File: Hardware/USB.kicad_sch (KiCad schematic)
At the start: 14 parts, among them J7 ??, U7 CP2102N-A02-GQFN24

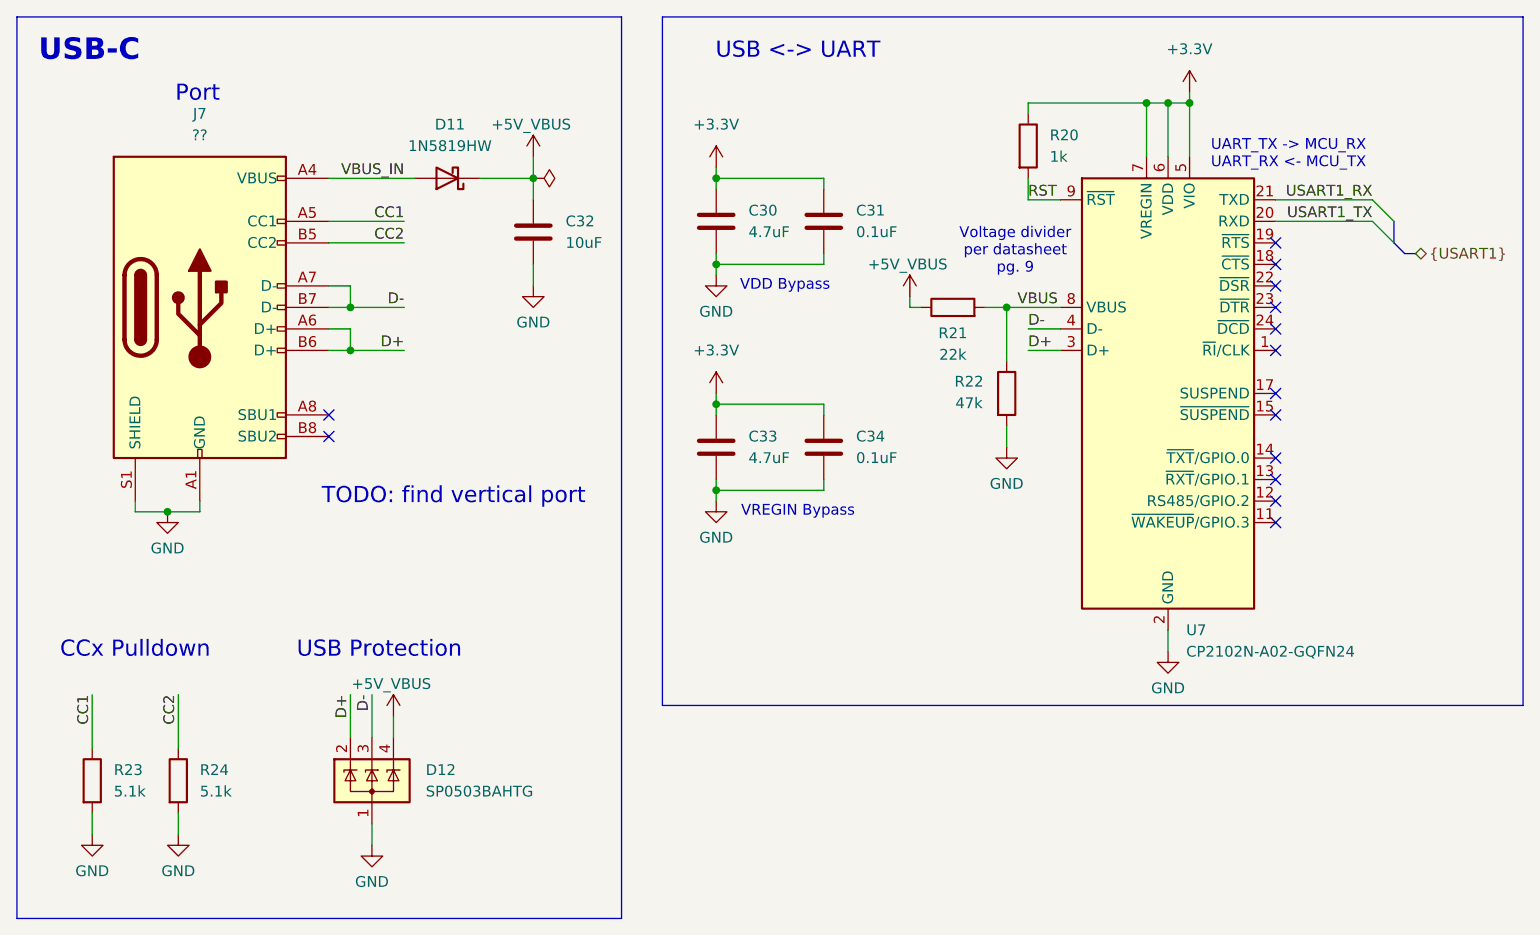
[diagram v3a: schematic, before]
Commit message: 0603 footprints
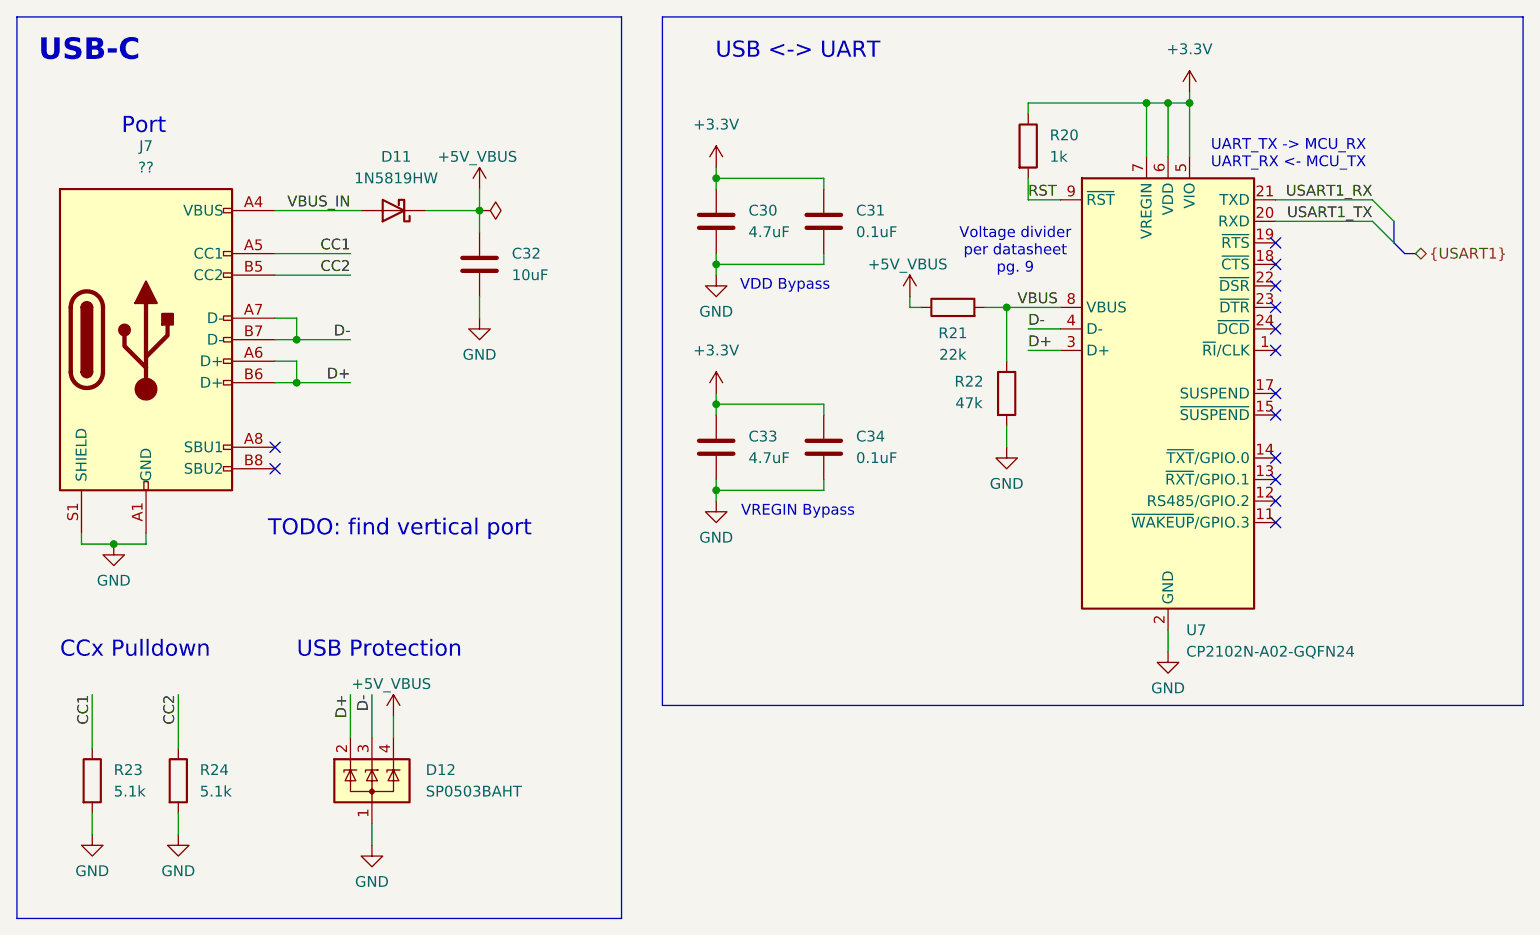
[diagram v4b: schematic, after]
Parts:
- removed D12: SP0503BAHTG, Package_TO_SOT_SMD:SOT-143, symbol utsvt_ics:SP0503BAH
- removed U7: CP2102N-A02-GQFN24, UTSVT_ICs:CP2102N-A02-GQFN24, symbol utsvt_ics:CP2102N-Axx-xQFN24
- added D12: SP0503BAHT, Package_TO_SOT_SMD:SOT-143, symbol utsvt-ics:SP0503BAH
- added U7: CP2102N-A02-GQFN24, UTSVT_ICs:CP2102N-A02-GQFN24, symbol utsvt-ics:CP2102N-Axx-xQFN24
- C30, C32, C33: footprint Capacitor_SMD:C_0805_2012Metric_Pad1.18x1.45mm_HandSolder -> Capacitor_SMD:C_0603_1608Metric_Pad1.08x0.95mm_HandSolder
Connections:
- net +3.3V: now also U7.5 (VIO), U7.6 (VDD), U7.7 (VREGIN)
- net +5V_VBUS: now also D12.4 (K)
- net D+: now also D12.2 (K), U7.3 (D+)
- net D-: now also D12.3 (K), U7.4 (D-)
- net GND: now also D12.1 (A), U7.2 (GND), U7.25 (GND)
- net RST: now also U7.9 (~{RST})
- net USART1_RX: now also U7.21 (TXD)
- net USART1_TX: now also U7.20 (RXD)
- net VBUS: now also U7.8 (VBUS)
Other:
- moved on the sheet: C32, D11, J7

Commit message: 24-5 buck from psom, OR gate for bootload. more sheet organization
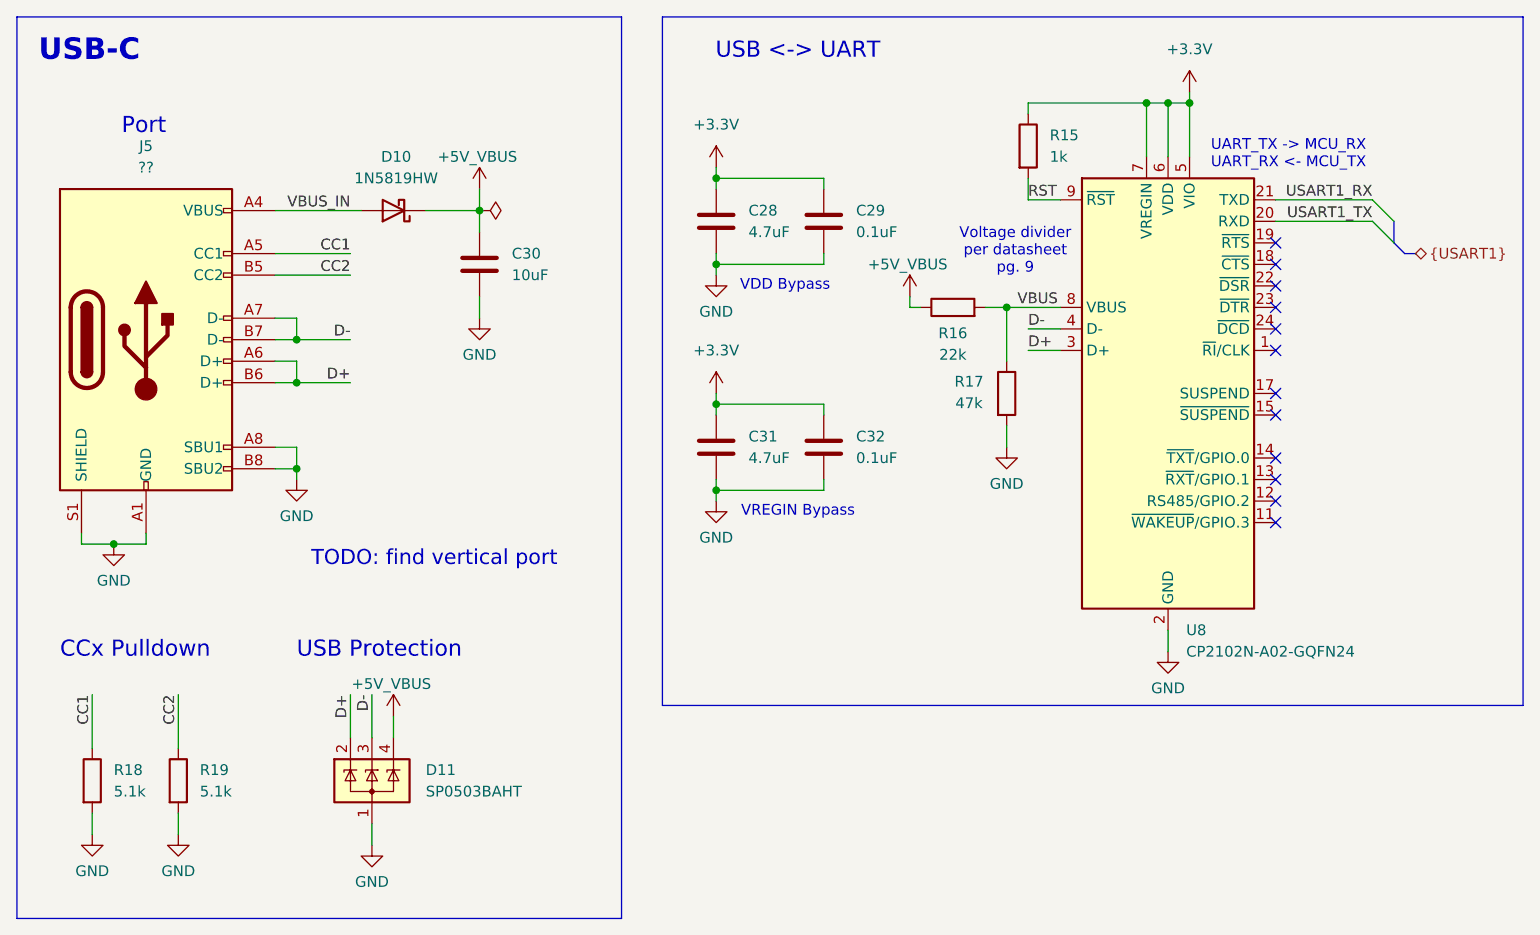
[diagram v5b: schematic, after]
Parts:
- renumbered C30 to C28, C31 to C29, C32 to C30, C33 to C31, C34 to C32, D11 to D10, D12 to D11, J7 to J5, R20 to R15, R21 to R16, R22 to R17, R23 to R18, R24 to R19, U7 to U8
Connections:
- net GND: now also J5.A8 (SBU1), J5.B8 (SBU2)
- no-connect marks 14 -> 12

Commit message: changed to 2 channel op amp, stole RPP from PSOM
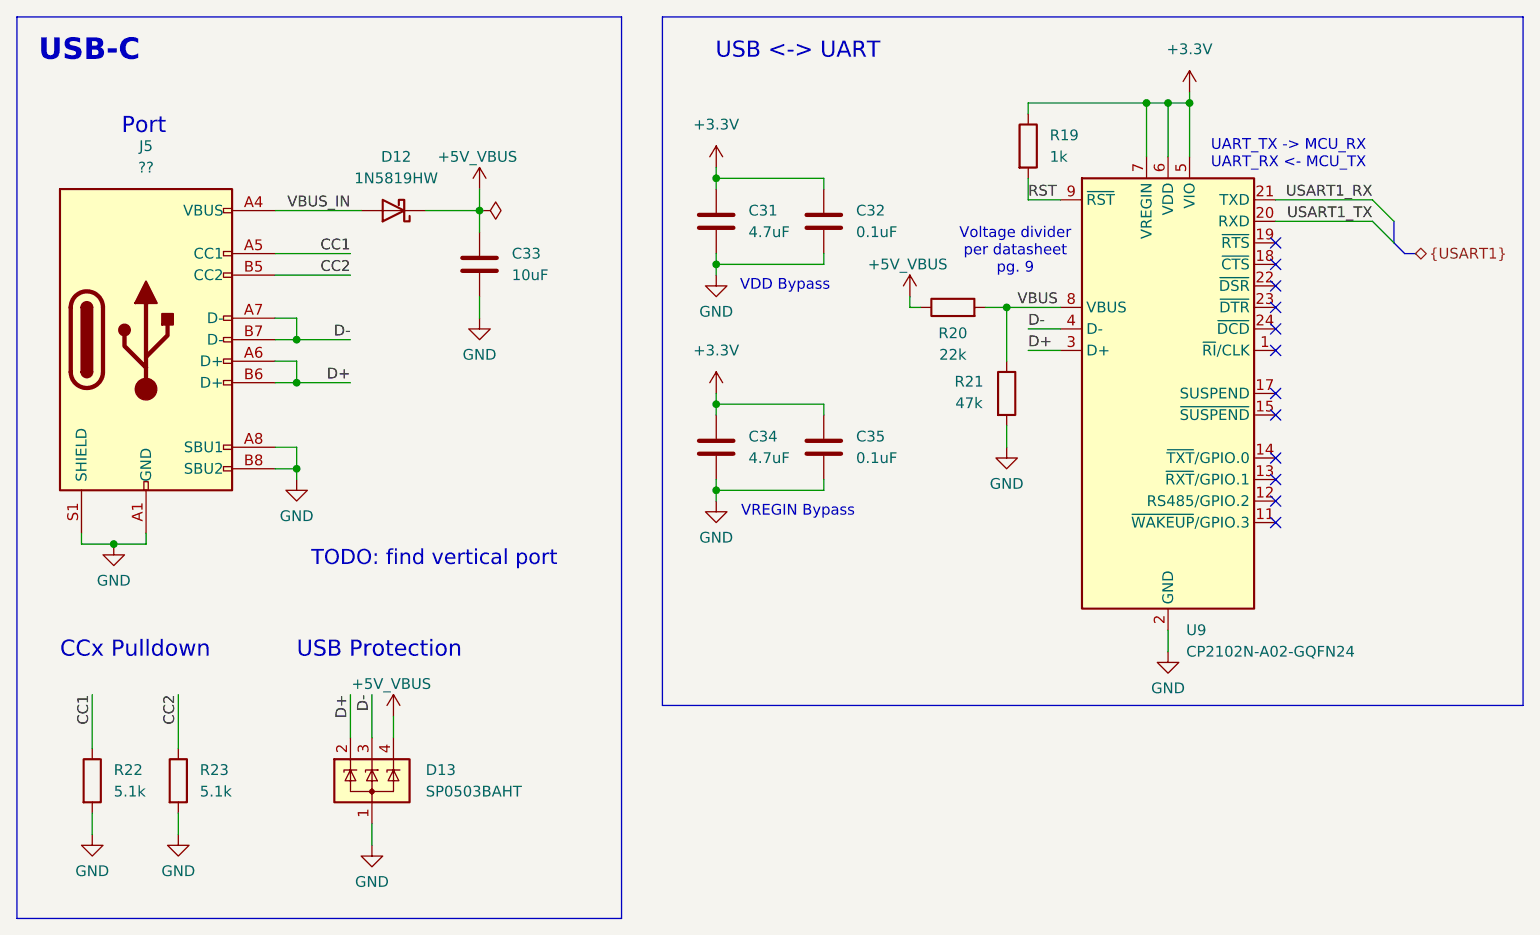
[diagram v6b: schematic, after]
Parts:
- renumbered C28 to C31, C29 to C32, C30 to C33, C31 to C34, C32 to C35, D10 to D12, D11 to D13, R15 to R19, R16 to R20, R17 to R21, R18 to R22, R19 to R23, U8 to U9

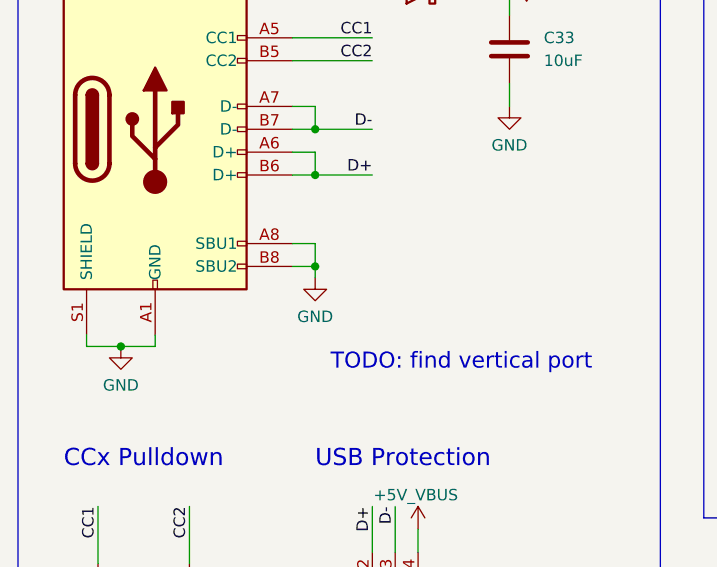
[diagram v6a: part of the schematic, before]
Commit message: added voltage reference, shunt model; addressed comments
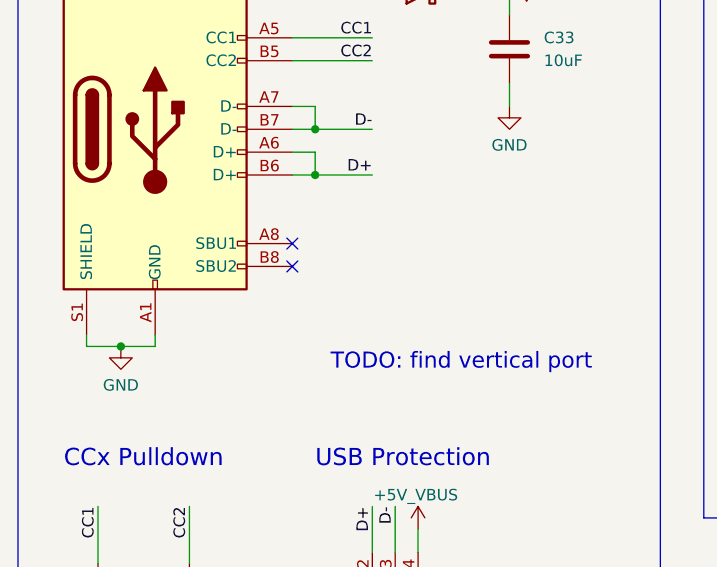
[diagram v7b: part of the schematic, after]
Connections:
- net GND: no longer J5.A8 (SBU1), J5.B8 (SBU2)
- no-connect marks 12 -> 14
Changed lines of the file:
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@@
 	)
 	(junction
-		(at 48.26 68.58)
-		(diameter 0)
-		(color 0 0 0 0)
-	)
-	(junction
 		(at 148.59 25.4)
 		(diameter 0)
@@
 	)
 	(no_connect
+		(at 45.72 66.04)
+	)
+	(no_connect
 		(at 163.83 62.23)
 	)
@@
 	)
 	(no_connect
+		(at 45.72 68.58)
+	)
+	(no_connect
 		(at 163.83 69.85)
 	)
@@
 	(wire
 		(pts
-			(xy 45.72 68.58) (xy 48.26 68.58)
-		)
-		(stroke
-			(width 0)
-			(type default)
-		)
-	)
-	(wire
-		(pts
 			(xy 134.62 26.67) (xy 134.62 25.4)
 		)
@@
 	(wire
 		(pts
-			(xy 48.26 68.58) (xy 48.26 69.85)
-		)
-		(stroke
-			(width 0)
-			(type default)
-		)
-	)
-	(wire
-		(pts
 			(xy 153.67 24.13) (xy 153.67 25.4)
 		)
@@
 	(wire
 		(pts
-			(xy 48.26 66.04) (xy 48.26 68.58)
-		)
-		(stroke
-			(width 0)
-			(type default)
-		)
-	)
-	(wire
-		(pts
 			(xy 134.62 52.07) (xy 138.43 52.07)
 		)
@@
 	(wire
 		(pts
-			(xy 45.72 66.04) (xy 48.26 66.04)
-		)
-		(stroke
-			(width 0)
-			(type default)
-		)
-	)
-	(wire
-		(pts
 			(xy 45.72 38.1) (xy 55.88 38.1)
 		)
@@
 		(on_board yes)
 		(dnp no)
-		(property "Reference" "#PWR081"
+		(property "Reference" "#PWR082"
 			(at 69.85 39.37 0)
 			(effects
@@
 			(project "BPS-AmperesPCB"
 				(path "/a452d214-ea00-440d-a445-5d6103fda43a/c14a2c5c-255b-423f-b086-532f80606e87"
-					(reference "#PWR081")
+					(reference "#PWR082")
 					(unit 1)
 				)
@@
 		(on_board yes)
 		(dnp no)
-		(property "Reference" "#PWR083"
+		(property "Reference" "#PWR084"
 			(at 120.65 52.07 0)
 			(effects
@@
 			(project "BPS-AmperesPCB"
 				(path "/a452d214-ea00-440d-a445-5d6103fda43a/c14a2c5c-255b-423f-b086-532f80606e87"
-					(reference "#PWR083")
+					(reference "#PWR084")
 					(unit 1)
 				)
@@
 		(on_board yes)
 		(dnp no)
-		(property "Reference" "#PWR084"
+		(property "Reference" "#PWR085"
 			(at 69.85 57.15 0)
 			(effects
@@
 			(project "BPS-AmperesPCB"
 				(path "/a452d214-ea00-440d-a445-5d6103fda43a/c14a2c5c-255b-423f-b086-532f80606e87"
-					(reference "#PWR084")
+					(reference "#PWR085")
 					(unit 1)
 				)
@@
 		(on_board yes)
 		(dnp no)
-		(property "Reference" "#PWR090"
+		(property "Reference" "#PWR091"
 			(at 151.13 96.52 0)
 			(effects
@@
 			(project "BPS-AmperesPCB"
 				(path "/a452d214-ea00-440d-a445-5d6103fda43a/c14a2c5c-255b-423f-b086-532f80606e87"
-					(reference "#PWR090")
+					(reference "#PWR091")
 					(unit 1)
 				)
@@
 		(dnp no)
 		(fields_autoplaced yes)
-		(property "Reference" "#FLG07"
+		(property "Reference" "#FLG06"
 			(at 71.755 38.1 0)
 			(effects
@@
 			(project "BPS-AmperesPCB"
 				(path "/a452d214-ea00-440d-a445-5d6103fda43a/c14a2c5c-255b-423f-b086-532f80606e87"
-					(reference "#FLG07")
+					(reference "#FLG06")
 					(unit 1)
 				)
@@
 		(on_board yes)
 		(dnp no)
-		(property "Reference" "#PWR091"
+		(property "Reference" "#PWR092"
 			(at 59.69 101.6 0)
 			(effects
@@
 			(project "BPS-AmperesPCB"
 				(path "/a452d214-ea00-440d-a445-5d6103fda43a/c14a2c5c-255b-423f-b086-532f80606e87"
-					(reference "#PWR091")
+					(reference "#PWR092")
 					(unit 1)
 				)
@@
 		(dnp no)
 		(fields_autoplaced yes)
-		(property "Reference" "#PWR079"
+		(property "Reference" "#PWR080"
 			(at 153.67 27.94 0)
 			(effects
@@
 			(project "BPS-AmperesPCB"
 				(path "/a452d214-ea00-440d-a445-5d6103fda43a/c14a2c5c-255b-423f-b086-532f80606e87"
-					(reference "#PWR079")
+					(reference "#PWR080")
 					(unit 1)
 				)
@@
 		(dnp no)
 		(fields_autoplaced yes)
-		(property "Reference" "#PWR085"
+		(property "Reference" "#PWR086"
 			(at 97.79 63.5 0)
 			(effects
@@
 			(project "BPS-AmperesPCB"
 				(path "/a452d214-ea00-440d-a445-5d6103fda43a/c14a2c5c-255b-423f-b086-532f80606e87"
-					(reference "#PWR085")
+					(reference "#PWR086")
 					(unit 1)
 				)
@@
 		(on_board yes)
 		(dnp no)
-		(property "Reference" "#PWR094"
+		(property "Reference" "#PWR095"
 			(at 57.15 119.38 0)
 			(effects
@@
 			(project "BPS-AmperesPCB"
 				(path "/a452d214-ea00-440d-a445-5d6103fda43a/c14a2c5c-255b-423f-b086-532f80606e87"
-					(reference "#PWR094")
+					(reference "#PWR095")
 					(unit 1)
 				)
@@
 		(dnp no)
 		(fields_autoplaced yes)
-		(property "Reference" "#PWR080"
+		(property "Reference" "#PWR081"
 			(at 97.79 36.83 0)
 			(effects
@@
 			(project "BPS-AmperesPCB"
 				(path "/a452d214-ea00-440d-a445-5d6103fda43a/c14a2c5c-255b-423f-b086-532f80606e87"
-					(reference "#PWR080")
+					(reference "#PWR081")
 					(unit 1)
 				)
@@
 		(on_board yes)
 		(dnp no)
-		(property "Reference" "#PWR093"
+		(property "Reference" "#PWR094"
 			(at 34.29 118.11 0)
 			(effects
@@
 			(project "BPS-AmperesPCB"
 				(path "/a452d214-ea00-440d-a445-5d6103fda43a/c14a2c5c-255b-423f-b086-532f80606e87"
-					(reference "#PWR093")
+					(reference "#PWR094")
 					(unit 1)
 				)
@@
 		(on_board yes)
 		(dnp no)
-		(property "Reference" "#PWR082"
+		(property "Reference" "#PWR083"
 			(at 97.79 52.07 0)
 			(effects
@@
 			(project "BPS-AmperesPCB"
 				(path "/a452d214-ea00-440d-a445-5d6103fda43a/c14a2c5c-255b-423f-b086-532f80606e87"
-					(reference "#PWR082")
+					(reference "#PWR083")
 					(unit 1)
 				)
@@
 		(on_board yes)
 		(dnp no)
-		(property "Reference" "#PWR088"
+		(property "Reference" "#PWR089"
 			(at 97.79 78.74 0)
 			(effects
@@
 			(project "BPS-AmperesPCB"
 				(path "/a452d214-ea00-440d-a445-5d6103fda43a/c14a2c5c-255b-423f-b086-532f80606e87"
-					(reference "#PWR088")
+					(reference "#PWR089")
 					(unit 1)
 				)
@@
 		(on_board yes)
 		(dnp no)
-		(property "Reference" "#PWR092"
+		(property "Reference" "#PWR093"
 			(at 24.13 118.11 0)
 			(effects
@@
 			(project "BPS-AmperesPCB"
 				(path "/a452d214-ea00-440d-a445-5d6103fda43a/c14a2c5c-255b-423f-b086-532f80606e87"
-					(reference "#PWR092")
+					(reference "#PWR093")
 					(unit 1)
 				)
@@
 		(on_board yes)
 		(dnp no)
-		(property "Reference" "#PWR086"
+		(property "Reference" "#PWR087"
 			(at 132.08 72.39 0)
 			(effects
@@
 			(project "BPS-AmperesPCB"
 				(path "/a452d214-ea00-440d-a445-5d6103fda43a/c14a2c5c-255b-423f-b086-532f80606e87"
-					(reference "#PWR086")
+					(reference "#PWR087")
 					(unit 1)
 				)
@@
 		(on_board yes)
 		(dnp no)
-		(property "Reference" "#PWR089"
+		(property "Reference" "#PWR090"
 			(at 26.67 83.82 0)
 			(effects
@@
 			(project "BPS-AmperesPCB"
 				(path "/a452d214-ea00-440d-a445-5d6103fda43a/c14a2c5c-255b-423f-b086-532f80606e87"
-					(reference "#PWR089")
-					(unit 1)
-				)
-			)
-		)
-	)
-	(symbol
-		(lib_id "power:GND")
-		(at 48.26 69.85 0)
-		(unit 1)
-		(exclude_from_sim no)
-		(in_bom yes)
-		(on_board yes)
-		(dnp no)
-		(property "Reference" "#PWR087"
-			(at 48.26 76.2 0)
-			(effects
-				(font
-					(size 1.27 1.27)
-				)
-				(hide yes)
-			)
-		)
-		(property "Value" "GND"
-			(at 48.26 74.168 0)
-			(effects
-				(font
-					(size 1.27 1.27)
-				)
-			)
-		)
-		(property "Footprint" ""
-			(at 48.26 69.85 0)
-			(effects
-				(font
-					(size 1.27 1.27)
-				)
-				(hide yes)
-			)
-		)
-		(property "Datasheet" ""
-			(at 48.26 69.85 0)
-			(effects
-				(font
-					(size 1.27 1.27)
-				)
-				(hide yes)
-			)
-		)
-		(property "Description" "Power symbol creates a global label with name \"GND\" , ground"
-			(at 48.26 69.85 0)
-			(effects
-				(font
-					(size 1.27 1.27)
-				)
-				(hide yes)
-			)
-		)
-		(pin "1"
-		)
-		(instances
-			(project "BPS-AmperesPCB"
-				(path "/a452d214-ea00-440d-a445-5d6103fda43a/c14a2c5c-255b-423f-b086-532f80606e87"
-					(reference "#PWR087")
+					(reference "#PWR090")
 					(unit 1)
 				)
